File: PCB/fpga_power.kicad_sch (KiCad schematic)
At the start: 11 parts, among them U4 LFE5U-25F-6BG256C

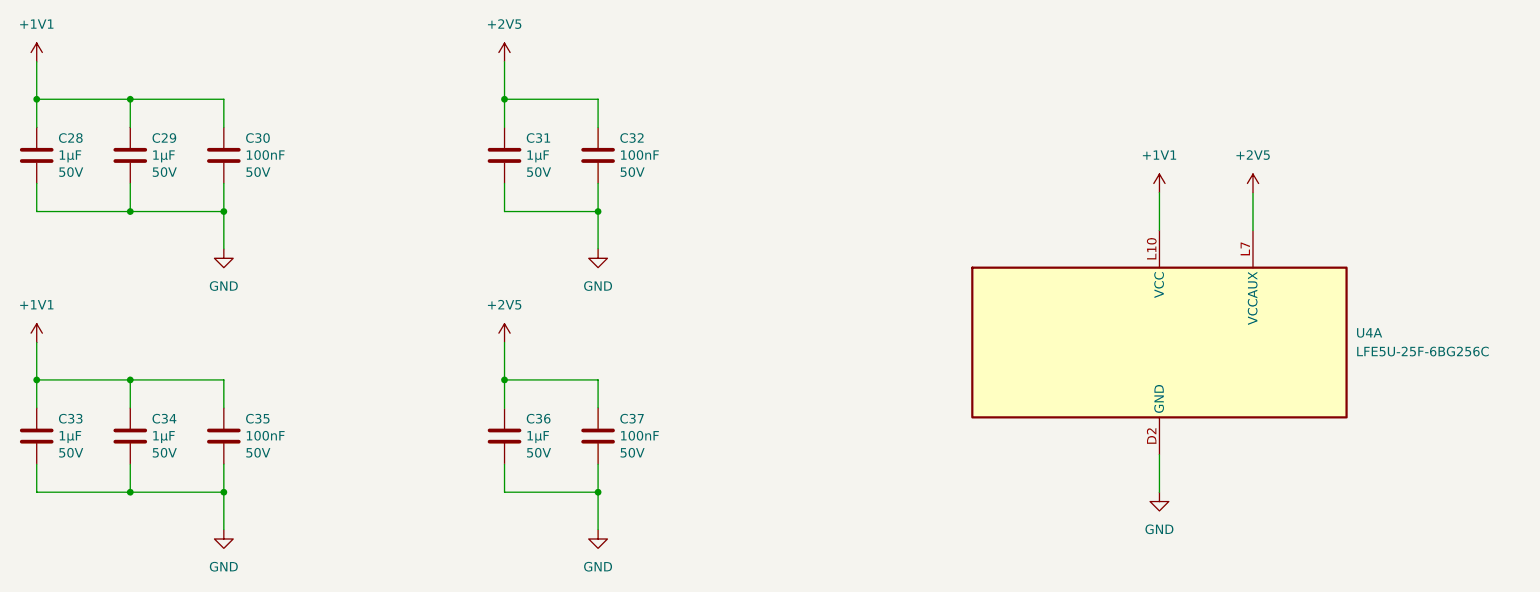
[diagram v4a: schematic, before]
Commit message: Add LICENSE and minor improvements
- Filled the title blocks
- Connected the LEDs to the FPGA
- Changed the FPGA programming header
- Added USB fuse and capacitors
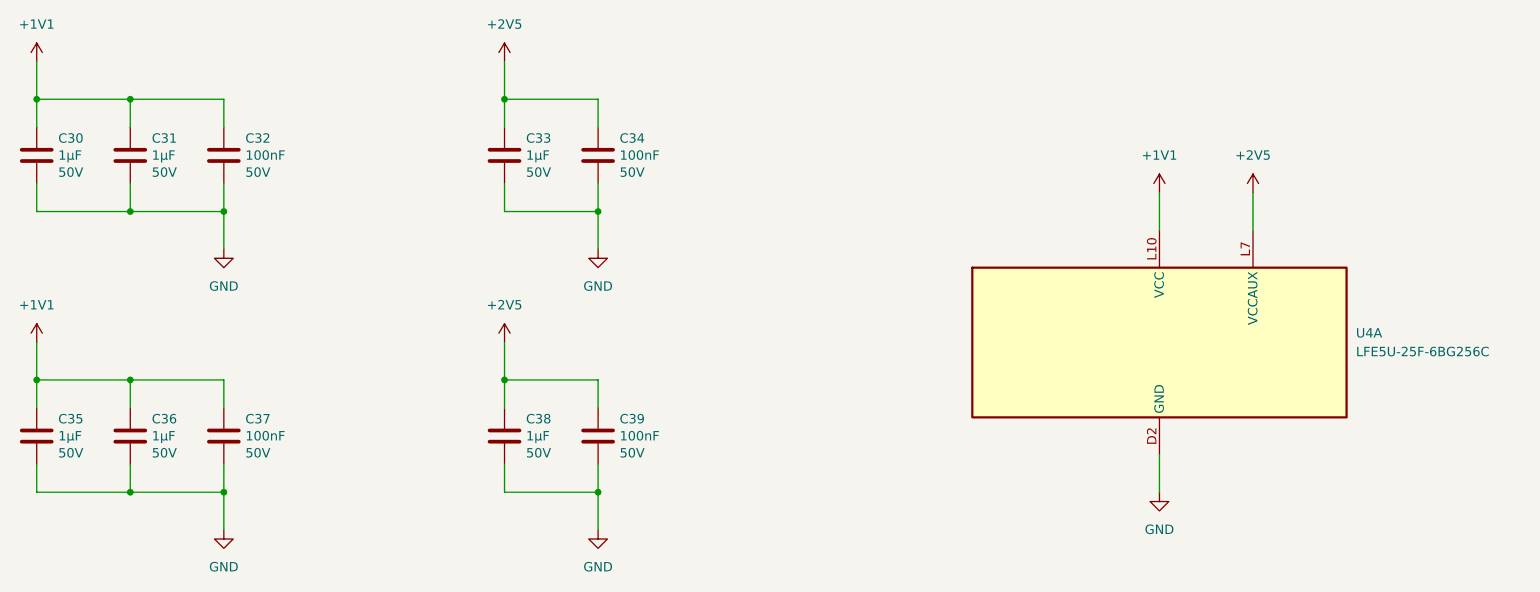
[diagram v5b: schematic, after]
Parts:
- renumbered C28 to C30, C29 to C31, C30 to C32, C31 to C33, C32 to C34, C33 to C35, C34 to C36, C35 to C37, C36 to C38, C37 to C39
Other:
- company: (none) -> Copyright (c) 2025 L. Sartory
- title: (none) -> Clavier - FPGA power
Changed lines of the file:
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@@
 	(generator_version "9.0")
 	(paper "A4")
+	(title_block
+		(title "Clavier - FPGA power")
+		(date "2025-06-01")
+		(rev "1.0")
+		(company "Copyright (c) 2025 L. Sartory")
+		(comment 1 "SPDX-License-Identifier: CERN-OHL-P-2.0")
+	)
 	(junction
 		(at 76.2 109.22)
@@
 		(on_board yes)
 		(dnp no)
-		(property "Reference" "C28"
+		(property "Reference" "C30"
 			(at 53.721 61.1886 0)
 			(effects
@@
 			(project "clavier"
 				(path "/6362c6e0-59ef-40d3-b6e0-7e9dfe7b9b20/d73938da-f0ba-48e3-aac9-a36988c25c2c/e36c52fe-7af8-49a0-bf3c-a636c30fc9cb"
-					(reference "C28")
+					(reference "C30")
 					(unit 1)
 				)
@@
 		(on_board yes)
 		(dnp no)
-		(property "Reference" "C30"
+		(property "Reference" "C32"
 			(at 79.121 61.1886 0)
 			(effects
@@
 			(project "clavier"
 				(path "/6362c6e0-59ef-40d3-b6e0-7e9dfe7b9b20/d73938da-f0ba-48e3-aac9-a36988c25c2c/e36c52fe-7af8-49a0-bf3c-a636c30fc9cb"
-					(reference "C30")
+					(reference "C32")
 					(unit 1)
 				)
@@
 		(on_board yes)
 		(dnp no)
-		(property "Reference" "C29"
+		(property "Reference" "C31"
 			(at 66.421 61.1886 0)
 			(effects
@@
 			(project "clavier"
 				(path "/6362c6e0-59ef-40d3-b6e0-7e9dfe7b9b20/d73938da-f0ba-48e3-aac9-a36988c25c2c/e36c52fe-7af8-49a0-bf3c-a636c30fc9cb"
-					(reference "C29")
+					(reference "C31")
 					(unit 1)
 				)
@@
 		(on_board yes)
 		(dnp no)
-		(property "Reference" "C34"
+		(property "Reference" "C36"
 			(at 66.421 99.2886 0)
 			(effects
@@
 			(project "clavier"
 				(path "/6362c6e0-59ef-40d3-b6e0-7e9dfe7b9b20/d73938da-f0ba-48e3-aac9-a36988c25c2c/e36c52fe-7af8-49a0-bf3c-a636c30fc9cb"
-					(reference "C34")
+					(reference "C36")
 					(unit 1)
 				)
@@
 		(on_board yes)
 		(dnp no)
-		(property "Reference" "C36"
+		(property "Reference" "C38"
 			(at 117.221 99.2886 0)
 			(effects
@@
 			(project "clavier"
 				(path "/6362c6e0-59ef-40d3-b6e0-7e9dfe7b9b20/d73938da-f0ba-48e3-aac9-a36988c25c2c/e36c52fe-7af8-49a0-bf3c-a636c30fc9cb"
-					(reference "C36")
+					(reference "C38")
 					(unit 1)
 				)
@@
 		(on_board yes)
 		(dnp no)
-		(property "Reference" "C31"
+		(property "Reference" "C33"
 			(at 117.221 61.1886 0)
 			(effects
@@
 			(project "clavier"
 				(path "/6362c6e0-59ef-40d3-b6e0-7e9dfe7b9b20/d73938da-f0ba-48e3-aac9-a36988c25c2c/e36c52fe-7af8-49a0-bf3c-a636c30fc9cb"
-					(reference "C31")
+					(reference "C33")
 					(unit 1)
 				)
@@
 		(dnp no)
 		(fields_autoplaced yes)
-		(property "Reference" "#PWR058"
+		(property "Reference" "#PWR057"
 			(at 114.3 54.61 0)
 			(effects
@@
 			(project "clavier"
 				(path "/6362c6e0-59ef-40d3-b6e0-7e9dfe7b9b20/d73938da-f0ba-48e3-aac9-a36988c25c2c/e36c52fe-7af8-49a0-bf3c-a636c30fc9cb"
-					(reference "#PWR058")
+					(reference "#PWR057")
 					(unit 1)
 				)
@@
 		(on_board yes)
 		(dnp no)
-		(property "Reference" "C37"
+		(property "Reference" "C39"
 			(at 129.921 99.2886 0)
 			(effects
@@
 			(project "clavier"
 				(path "/6362c6e0-59ef-40d3-b6e0-7e9dfe7b9b20/d73938da-f0ba-48e3-aac9-a36988c25c2c/e36c52fe-7af8-49a0-bf3c-a636c30fc9cb"
-					(reference "C37")
+					(reference "C39")
 					(unit 1)
 				)
@@
 		(dnp no)
 		(fields_autoplaced yes)
-		(property "Reference" "#PWR067"
+		(property "Reference" "#PWR066"
 			(at 127 120.65 0)
 			(effects
@@
 			(project "clavier"
 				(path "/6362c6e0-59ef-40d3-b6e0-7e9dfe7b9b20/d73938da-f0ba-48e3-aac9-a36988c25c2c/e36c52fe-7af8-49a0-bf3c-a636c30fc9cb"
-					(reference "#PWR067")
+					(reference "#PWR066")
 					(unit 1)
 				)
@@
 		(dnp no)
 		(fields_autoplaced yes)
-		(property "Reference" "#PWR060"
+		(property "Reference" "#PWR059"
 			(at 215.9 72.39 0)
 			(effects
@@
 			(project "clavier"
 				(path "/6362c6e0-59ef-40d3-b6e0-7e9dfe7b9b20/d73938da-f0ba-48e3-aac9-a36988c25c2c/e36c52fe-7af8-49a0-bf3c-a636c30fc9cb"
-					(reference "#PWR060")
+					(reference "#PWR059")
 					(unit 1)
 				)
@@
 		(dnp no)
 		(fields_autoplaced yes)
-		(property "Reference" "#PWR059"
+		(property "Reference" "#PWR058"
 			(at 203.2 72.39 0)
 			(effects
@@
 			(project "clavier"
 				(path "/6362c6e0-59ef-40d3-b6e0-7e9dfe7b9b20/d73938da-f0ba-48e3-aac9-a36988c25c2c/e36c52fe-7af8-49a0-bf3c-a636c30fc9cb"
-					(reference "#PWR059")
+					(reference "#PWR058")
 					(unit 1)
 				)
@@
 		(dnp no)
 		(fields_autoplaced yes)
-		(property "Reference" "#PWR062"
+		(property "Reference" "#PWR061"
 			(at 127 82.55 0)
 			(effects
@@
 			(project "clavier"
 				(path "/6362c6e0-59ef-40d3-b6e0-7e9dfe7b9b20/d73938da-f0ba-48e3-aac9-a36988c25c2c/e36c52fe-7af8-49a0-bf3c-a636c30fc9cb"
-					(reference "#PWR062")
+					(reference "#PWR061")
 					(unit 1)
 				)
@@
 		(dnp no)
 		(fields_autoplaced yes)
-		(property "Reference" "#PWR061"
+		(property "Reference" "#PWR060"
 			(at 76.2 82.55 0)
 			(effects
@@
 			(project "clavier"
 				(path "/6362c6e0-59ef-40d3-b6e0-7e9dfe7b9b20/d73938da-f0ba-48e3-aac9-a36988c25c2c/e36c52fe-7af8-49a0-bf3c-a636c30fc9cb"
-					(reference "#PWR061")
+					(reference "#PWR060")
 					(unit 1)
 				)
@@
 		(dnp no)
 		(fields_autoplaced yes)
-		(property "Reference" "#PWR057"
+		(property "Reference" "#PWR056"
 			(at 50.8 54.61 0)
 			(effects
@@
 			(project "clavier"
 				(path "/6362c6e0-59ef-40d3-b6e0-7e9dfe7b9b20/d73938da-f0ba-48e3-aac9-a36988c25c2c/e36c52fe-7af8-49a0-bf3c-a636c30fc9cb"
-					(reference "#PWR057")
+					(reference "#PWR056")
 					(unit 1)
 				)
@@
 		(on_board yes)
 		(dnp no)
-		(property "Reference" "C33"
+		(property "Reference" "C35"
 			(at 53.721 99.2886 0)
 			(effects
@@
 			(project "clavier"
 				(path "/6362c6e0-59ef-40d3-b6e0-7e9dfe7b9b20/d73938da-f0ba-48e3-aac9-a36988c25c2c/e36c52fe-7af8-49a0-bf3c-a636c30fc9cb"
-					(reference "C33")
+					(reference "C35")
 					(unit 1)
 				)
@@
 		(dnp no)
 		(fields_autoplaced yes)
-		(property "Reference" "#PWR065"
+		(property "Reference" "#PWR064"
 			(at 203.2 115.57 0)
 			(effects
@@
 			(project "clavier"
 				(path "/6362c6e0-59ef-40d3-b6e0-7e9dfe7b9b20/d73938da-f0ba-48e3-aac9-a36988c25c2c/e36c52fe-7af8-49a0-bf3c-a636c30fc9cb"
-					(reference "#PWR065")
+					(reference "#PWR064")
 					(unit 1)
 				)
@@
 		(dnp no)
 		(fields_autoplaced yes)
-		(property "Reference" "#PWR063"
+		(property "Reference" "#PWR062"
 			(at 50.8 92.71 0)
 			(effects
@@
 			(project "clavier"
 				(path "/6362c6e0-59ef-40d3-b6e0-7e9dfe7b9b20/d73938da-f0ba-48e3-aac9-a36988c25c2c/e36c52fe-7af8-49a0-bf3c-a636c30fc9cb"
-					(reference "#PWR063")
+					(reference "#PWR062")
 					(unit 1)
 				)
@@
 		(on_board yes)
 		(dnp no)
-		(property "Reference" "C32"
+		(property "Reference" "C34"
 			(at 129.921 61.1886 0)
 			(effects
@@
 			(project "clavier"
 				(path "/6362c6e0-59ef-40d3-b6e0-7e9dfe7b9b20/d73938da-f0ba-48e3-aac9-a36988c25c2c/e36c52fe-7af8-49a0-bf3c-a636c30fc9cb"
-					(reference "C32")
+					(reference "C34")
 					(unit 1)
 				)
@@
 		(dnp no)
 		(fields_autoplaced yes)
-		(property "Reference" "#PWR064"
+		(property "Reference" "#PWR063"
 			(at 114.3 92.71 0)
 			(effects
@@
 			(project "clavier"
 				(path "/6362c6e0-59ef-40d3-b6e0-7e9dfe7b9b20/d73938da-f0ba-48e3-aac9-a36988c25c2c/e36c52fe-7af8-49a0-bf3c-a636c30fc9cb"
-					(reference "#PWR064")
+					(reference "#PWR063")
 					(unit 1)
 				)
@@
 		(dnp no)
 		(fields_autoplaced yes)
-		(property "Reference" "#PWR066"
+		(property "Reference" "#PWR065"
 			(at 76.2 120.65 0)
 			(effects
@@
 			(project "clavier"
 				(path "/6362c6e0-59ef-40d3-b6e0-7e9dfe7b9b20/d73938da-f0ba-48e3-aac9-a36988c25c2c/e36c52fe-7af8-49a0-bf3c-a636c30fc9cb"
-					(reference "#PWR066")
+					(reference "#PWR065")
 					(unit 1)
 				)
@@
 		(on_board yes)
 		(dnp no)
-		(property "Reference" "C35"
+		(property "Reference" "C37"
 			(at 79.121 99.2886 0)
 			(effects
@@
 			(project "clavier"
 				(path "/6362c6e0-59ef-40d3-b6e0-7e9dfe7b9b20/d73938da-f0ba-48e3-aac9-a36988c25c2c/e36c52fe-7af8-49a0-bf3c-a636c30fc9cb"
-					(reference "C35")
+					(reference "C37")
 					(unit 1)
 				)

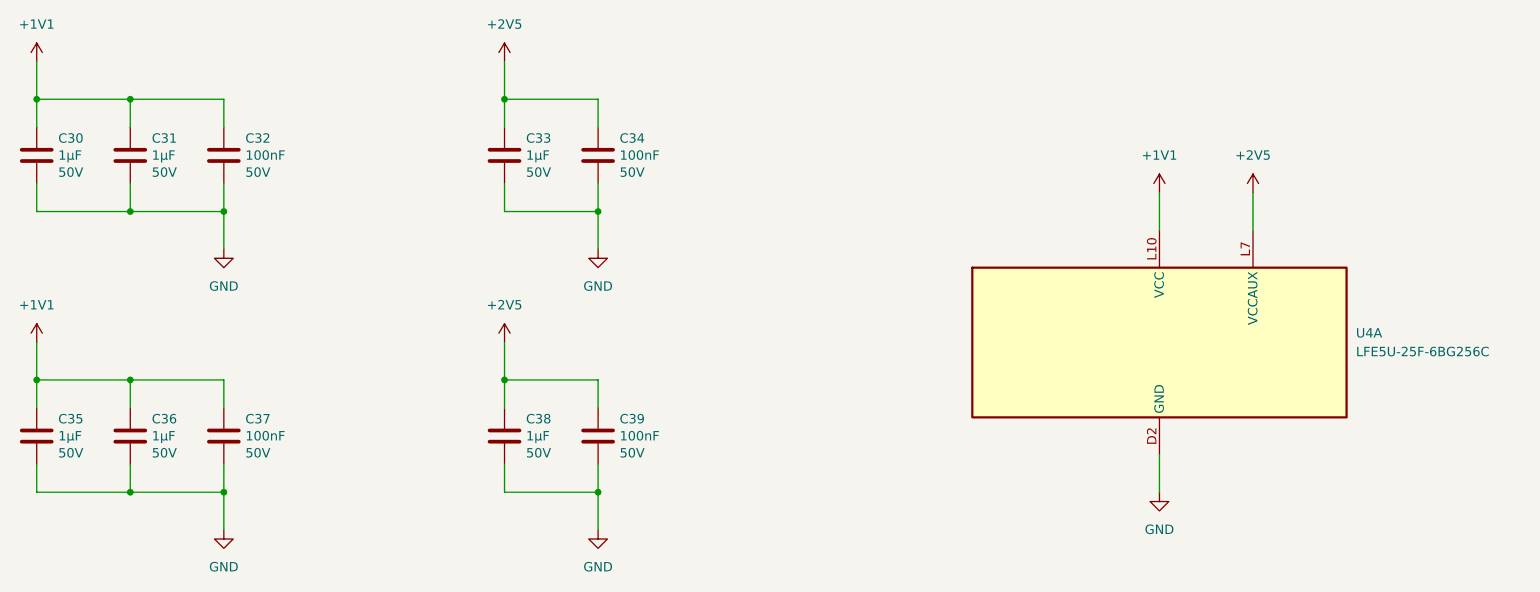
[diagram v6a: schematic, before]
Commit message: Place and route peripheral components
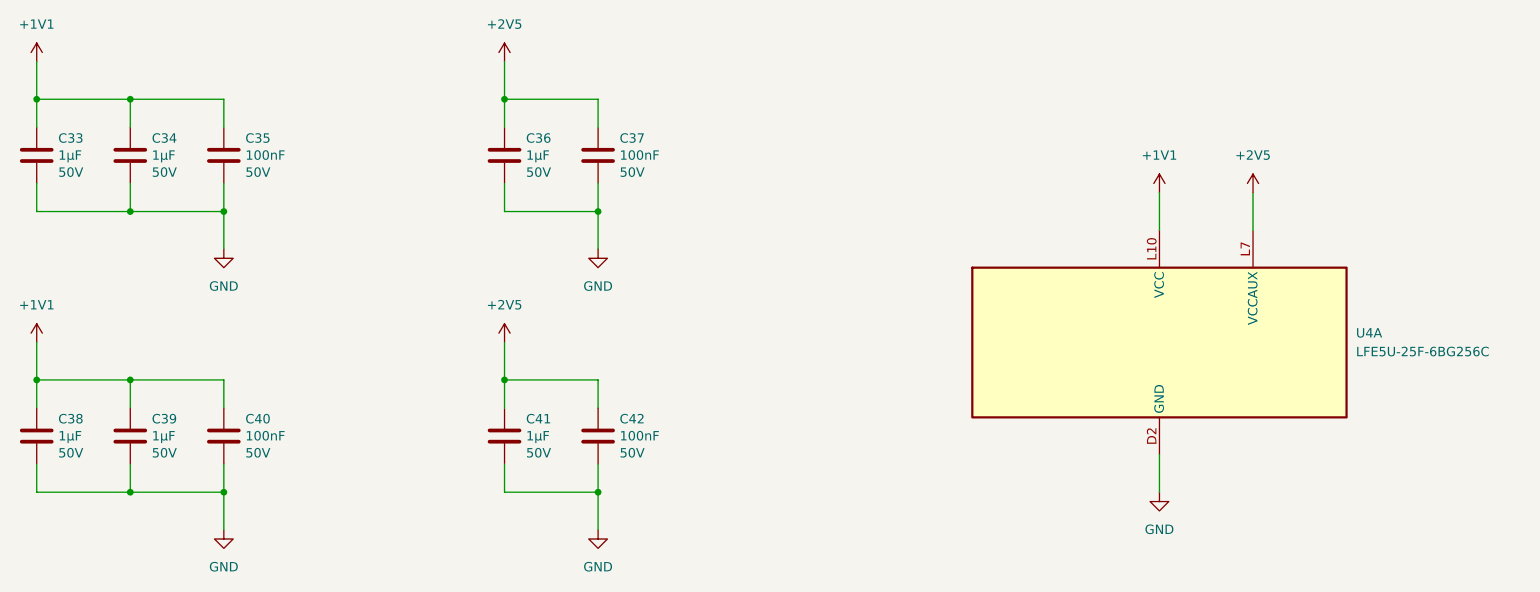
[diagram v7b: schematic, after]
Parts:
- renumbered C30 to C33, C31 to C34, C32 to C35, C33 to C36, C34 to C37, C35 to C38, C36 to C39, C37 to C40, C38 to C41, C39 to C42
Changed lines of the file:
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@@
 		(on_board yes)
 		(dnp no)
-		(property "Reference" "C30"
+		(property "Reference" "C33"
 			(at 53.721 61.1886 0)
 			(effects
@@
 			(project "clavier"
 				(path "/6362c6e0-59ef-40d3-b6e0-7e9dfe7b9b20/d73938da-f0ba-48e3-aac9-a36988c25c2c/e36c52fe-7af8-49a0-bf3c-a636c30fc9cb"
-					(reference "C30")
+					(reference "C33")
 					(unit 1)
 				)
@@
 		(on_board yes)
 		(dnp no)
-		(property "Reference" "C32"
+		(property "Reference" "C35"
 			(at 79.121 61.1886 0)
 			(effects
@@
 			(project "clavier"
 				(path "/6362c6e0-59ef-40d3-b6e0-7e9dfe7b9b20/d73938da-f0ba-48e3-aac9-a36988c25c2c/e36c52fe-7af8-49a0-bf3c-a636c30fc9cb"
-					(reference "C32")
+					(reference "C35")
 					(unit 1)
 				)
@@
 		(on_board yes)
 		(dnp no)
-		(property "Reference" "C31"
+		(property "Reference" "C34"
 			(at 66.421 61.1886 0)
 			(effects
@@
 			(project "clavier"
 				(path "/6362c6e0-59ef-40d3-b6e0-7e9dfe7b9b20/d73938da-f0ba-48e3-aac9-a36988c25c2c/e36c52fe-7af8-49a0-bf3c-a636c30fc9cb"
-					(reference "C31")
+					(reference "C34")
 					(unit 1)
 				)
@@
 		(on_board yes)
 		(dnp no)
-		(property "Reference" "C36"
+		(property "Reference" "C39"
 			(at 66.421 99.2886 0)
 			(effects
@@
 			(project "clavier"
 				(path "/6362c6e0-59ef-40d3-b6e0-7e9dfe7b9b20/d73938da-f0ba-48e3-aac9-a36988c25c2c/e36c52fe-7af8-49a0-bf3c-a636c30fc9cb"
-					(reference "C36")
+					(reference "C39")
 					(unit 1)
 				)
@@
 		(on_board yes)
 		(dnp no)
-		(property "Reference" "C38"
+		(property "Reference" "C41"
 			(at 117.221 99.2886 0)
 			(effects
@@
 			(project "clavier"
 				(path "/6362c6e0-59ef-40d3-b6e0-7e9dfe7b9b20/d73938da-f0ba-48e3-aac9-a36988c25c2c/e36c52fe-7af8-49a0-bf3c-a636c30fc9cb"
-					(reference "C38")
+					(reference "C41")
 					(unit 1)
 				)
@@
 		(on_board yes)
 		(dnp no)
-		(property "Reference" "C33"
+		(property "Reference" "C36"
 			(at 117.221 61.1886 0)
 			(effects
@@
 			(project "clavier"
 				(path "/6362c6e0-59ef-40d3-b6e0-7e9dfe7b9b20/d73938da-f0ba-48e3-aac9-a36988c25c2c/e36c52fe-7af8-49a0-bf3c-a636c30fc9cb"
-					(reference "C33")
+					(reference "C36")
 					(unit 1)
 				)
@@
 		(on_board yes)
 		(dnp no)
-		(property "Reference" "C39"
+		(property "Reference" "C42"
 			(at 129.921 99.2886 0)
 			(effects
@@
 			(project "clavier"
 				(path "/6362c6e0-59ef-40d3-b6e0-7e9dfe7b9b20/d73938da-f0ba-48e3-aac9-a36988c25c2c/e36c52fe-7af8-49a0-bf3c-a636c30fc9cb"
-					(reference "C39")
+					(reference "C42")
 					(unit 1)
 				)
@@
 		(on_board yes)
 		(dnp no)
-		(property "Reference" "C35"
+		(property "Reference" "C38"
 			(at 53.721 99.2886 0)
 			(effects
@@
 			(project "clavier"
 				(path "/6362c6e0-59ef-40d3-b6e0-7e9dfe7b9b20/d73938da-f0ba-48e3-aac9-a36988c25c2c/e36c52fe-7af8-49a0-bf3c-a636c30fc9cb"
-					(reference "C35")
+					(reference "C38")
 					(unit 1)
 				)
@@
 		(on_board yes)
 		(dnp no)
-		(property "Reference" "C34"
+		(property "Reference" "C37"
 			(at 129.921 61.1886 0)
 			(effects
@@
 			(project "clavier"
 				(path "/6362c6e0-59ef-40d3-b6e0-7e9dfe7b9b20/d73938da-f0ba-48e3-aac9-a36988c25c2c/e36c52fe-7af8-49a0-bf3c-a636c30fc9cb"
-					(reference "C34")
+					(reference "C37")
 					(unit 1)
 				)
@@
 		(on_board yes)
 		(dnp no)
-		(property "Reference" "C37"
+		(property "Reference" "C40"
 			(at 79.121 99.2886 0)
 			(effects
@@
 			(project "clavier"
 				(path "/6362c6e0-59ef-40d3-b6e0-7e9dfe7b9b20/d73938da-f0ba-48e3-aac9-a36988c25c2c/e36c52fe-7af8-49a0-bf3c-a636c30fc9cb"
-					(reference "C37")
+					(reference "C40")
 					(unit 1)
 				)

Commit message: Fan-out the FPGA
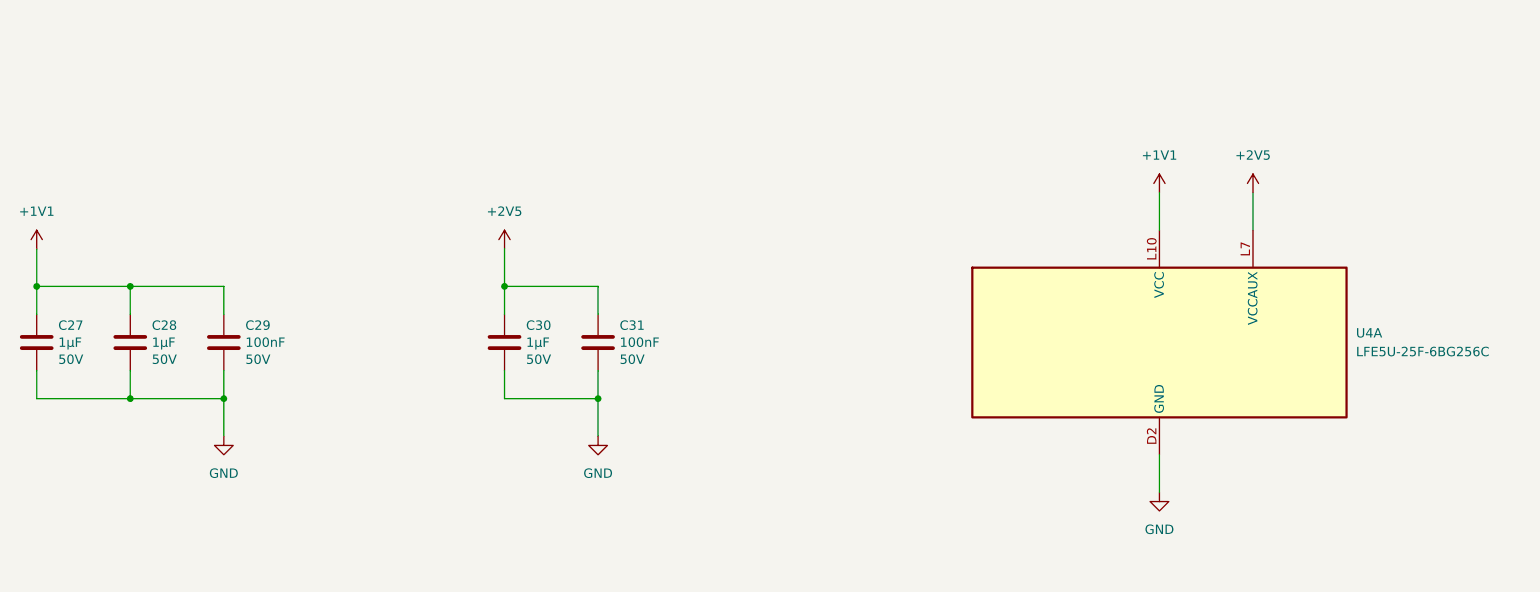
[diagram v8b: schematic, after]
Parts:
- removed C38, C39, C41: 1µF, Capacitor_SMD:C_0402_1005Metric_Pad0.74x0.62mm_HandSolder, symbol Device:C
- removed C40, C42: 100nF, Capacitor_SMD:C_0402_1005Metric_Pad0.74x0.62mm_HandSolder, symbol Device:C
- renumbered C33 to C27, C34 to C28, C35 to C29, C36 to C30, C37 to C31
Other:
- moved on the sheet: C27, C28, C29, C30, C31
